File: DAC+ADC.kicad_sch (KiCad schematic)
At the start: 103 parts, among them J3 Conn_01x02, U11 ZL38063, U12 W25Q16JVSS, U13 SN74LVC1G126DBV, U4 SN74LVC1G126DBV, Y1 12MHz

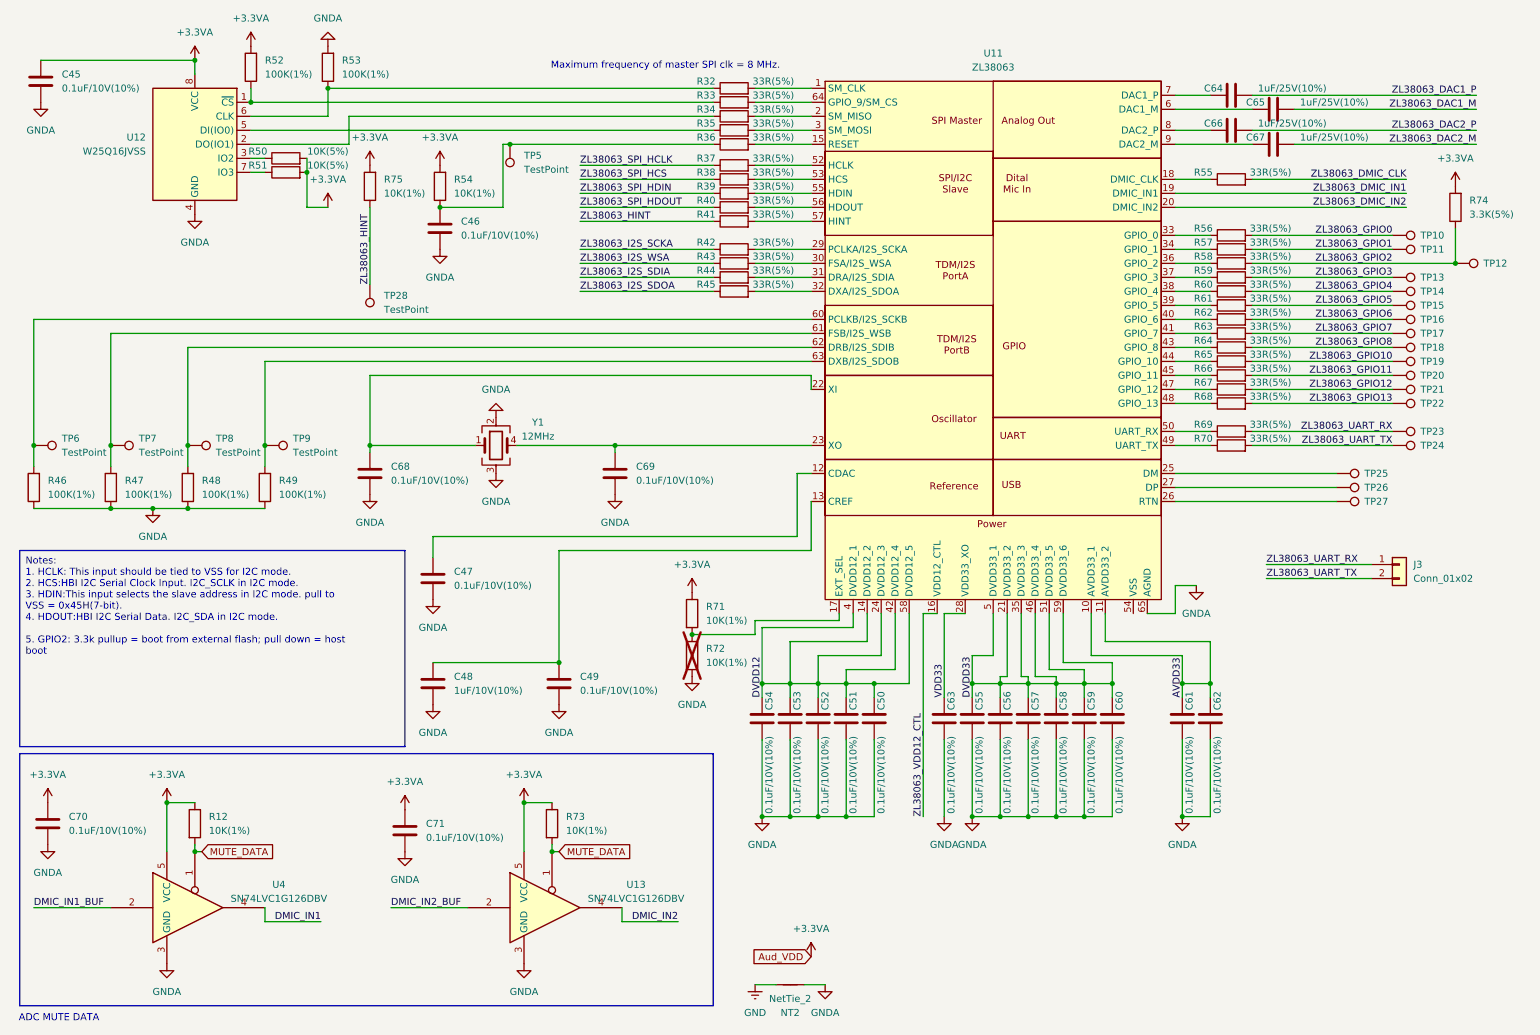
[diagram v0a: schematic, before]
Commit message: Added DSP, Neopixles, MIC's and mounting holes
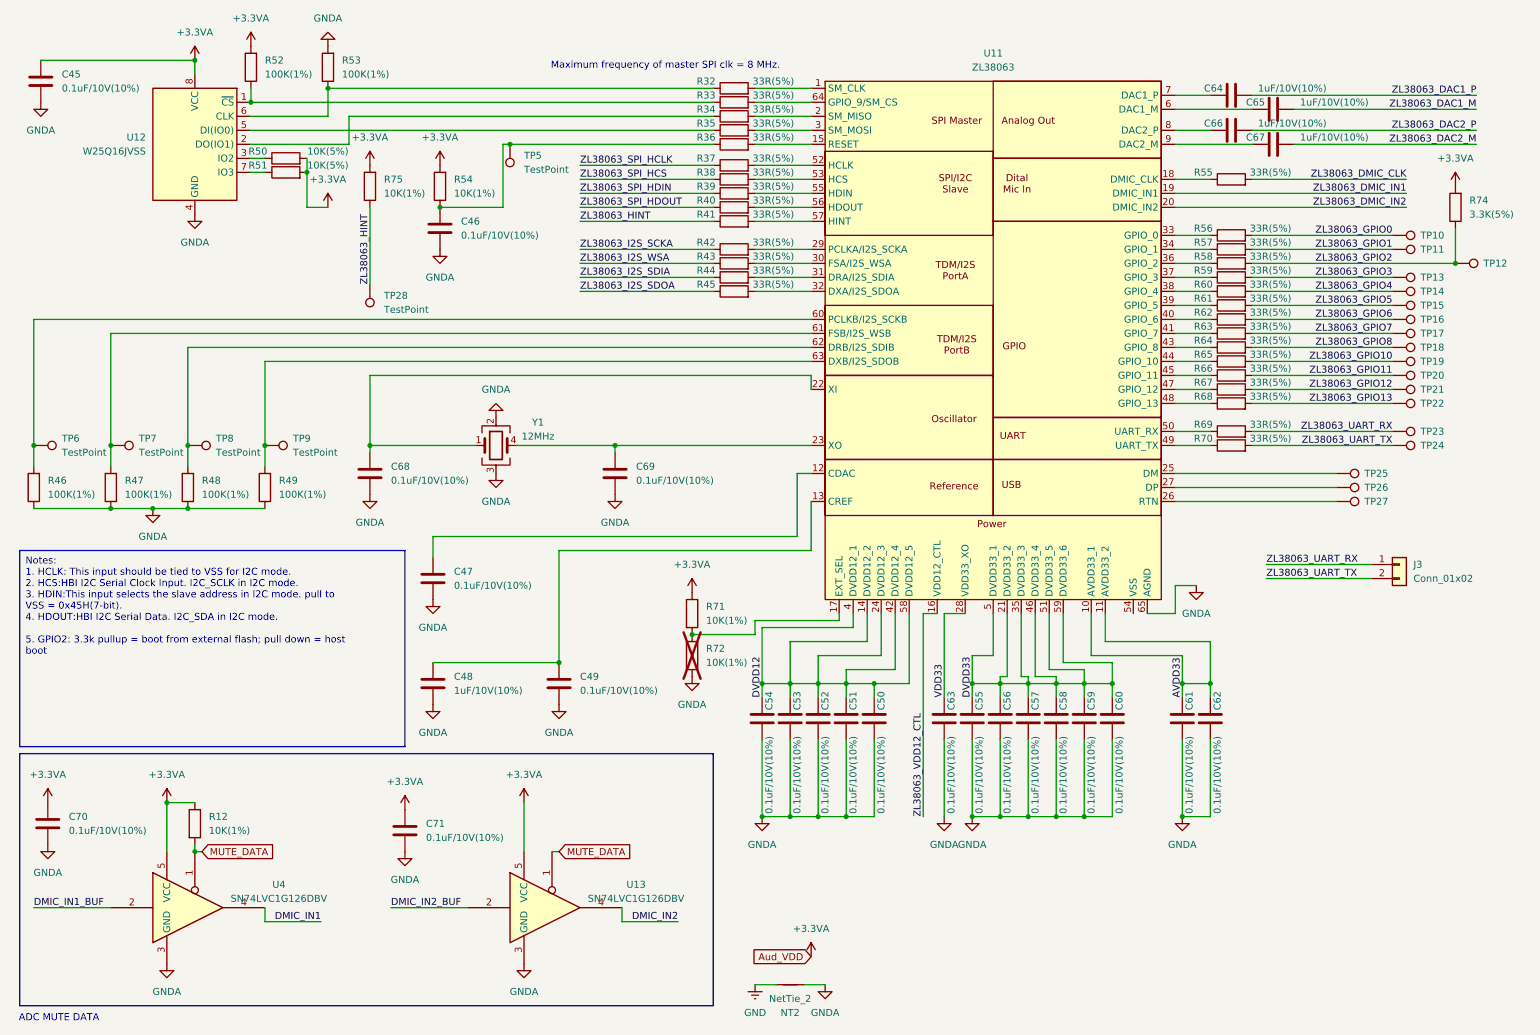
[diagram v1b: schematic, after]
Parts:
- removed R73: 10K(1%), Resistor_SMD:R_0603_1608Metric, symbol Device:R
- C45, C46, C47, C48, C49, C50, C51, C52, C53, C54, C55, C56, C57, C58, C59, C60, C61, C62, C63, C68, C69, C70, C71: footprint Capacitor_SMD:C_0603_1608Metric -> Capacitor_SMD:C_0402_1005Metric
- C64, C65, C66, C67: value 1uF/25V(10%) -> 1uF/10V(10%); footprint Capacitor_SMD:C_0603_1608Metric -> Capacitor_SMD:C_0402_1005Metric
- R12, R32, R33, R34, R35, R36, R37, R38, R39, R40, R41, R42, R43, R44, R45, R46, R47, R48, R49, R50, R51, R52, R53, R54, R55, R56, R57, R58, R59, R60, R61, R62, R63, R64, R65, R66, R67, R68, R69, R70, R71, R72, R74, R75: footprint Resistor_SMD:R_0603_1608Metric -> Resistor_SMD:R_0402_1005Metric
- TP10, TP11, TP12, TP13, TP14, TP15, TP16, TP17, TP18, TP19, TP20, TP21, TP22, TP23, TP24, TP25, TP26, TP27, TP28, TP5, TP6, TP7, TP8, TP9: footprint TestPoint:TestPoint_Pad_D1.5mm -> TestPoint:TestPoint_Pad_D1.0mm
- U12: footprint Package_SO:SOIC-8_5.23x5.23mm_P1.27mm -> Package_SO:SOIC-8_3.9x4.9mm_P1.27mm
- Y1: footprint Crystal:Crystal_SMD_7050-4Pin_7.0x5.0mm -> Crystal:Crystal_SMD_2520-4Pin_2.5x2.0mm
